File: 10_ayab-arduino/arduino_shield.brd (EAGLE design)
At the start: 69.9 x 54.6 mm, 20 parts, among them IC3 PCF8574T, IC4 PCF8574T

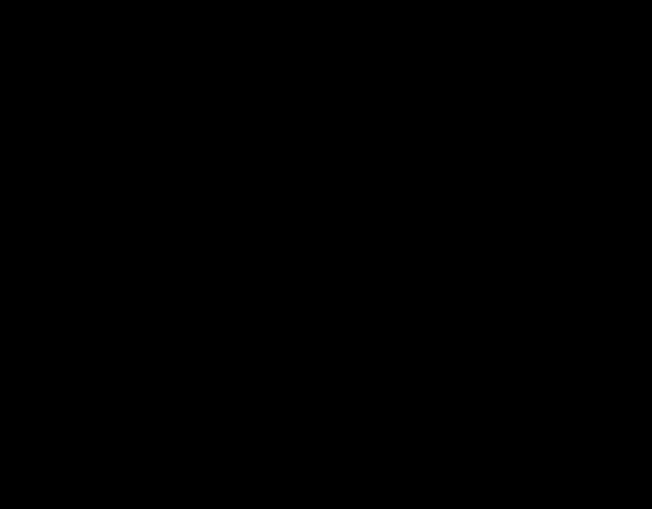
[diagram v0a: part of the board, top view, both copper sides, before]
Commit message: started work on improving shield, added reset button to schematic
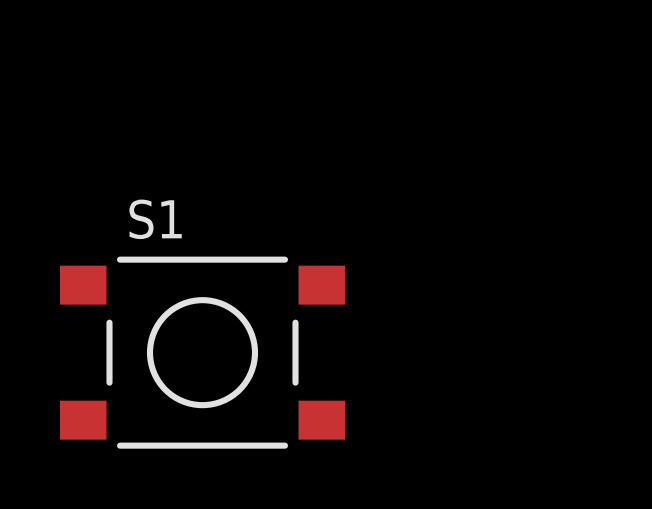
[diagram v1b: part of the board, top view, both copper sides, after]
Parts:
- added S1: DTSM-6, switch-tact:DTSM-6
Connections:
- new net RESET: ARD1.RST, S1.2
- net GND: now also S1.4
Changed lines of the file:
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@@
 <element name="U$1" library="frames" package="A4L-LOC" value="" x="-81.5975" y="-52.3875"/>
 <element name="JP6" library="pinhead" package="1X02" value="" x="39.0525" y="45.085" rot="R90"/>
+<element name="S1" library="switch-tact" package="DTSM-6" value="DTSM-6" x="-87.63" y="-47.625"/>
 </elements>
 <signals>
@@
 </signal>
 <signal name="GND">
-<contactref element="ARD1" pad="GND@1"/>
-<contactref element="ARD1" pad="GND@2"/>
-<contactref element="ARD1" pad="GND@3"/>
 <contactref element="IC3" pad="1"/>
 <contactref element="IC3" pad="2"/>
@@
 <contactref element="JP5" pad="10"/>
 <contactref element="LED1" pad="C"/>
-<contactref element="ARD1" pad="GND@1"/>
-<contactref element="ARD1" pad="GND@2"/>
 <contactref element="JP1" pad="P$2"/>
 <contactref element="JP1" pad="P$3"/>
@@
 <wire x1="18.0975" y1="8.255" x2="18.0975" y2="9.525" width="0.6096" layer="16"/>
 <wire x1="15.72" y1="7.62" x2="5.08" y2="7.62" width="0.6096" layer="16"/>
+<contactref element="ARD1" pad="GND@1"/>
+<contactref element="ARD1" pad="GND@2"/>
+<contactref element="ARD1" pad="GND@3"/>
+<contactref element="ARD1" pad="GND@1"/>
+<contactref element="ARD1" pad="GND@2"/>
+<contactref element="S1" pad="4"/>
+<wire x1="5.08" y1="7.62" x2="-83.655" y2="-49.875" width="0" layer="19" extent="1-1"/>
+<wire x1="5.08" y1="12.62" x2="5.08" y2="7.62" width="0" layer="19" extent="1-1"/>
+<wire x1="31.115" y1="22.86" x2="18.0975" y2="15.875" width="0" layer="19" extent="16-16"/>
+<wire x1="40.485" y1="16.51" x2="31.115" y2="22.86" width="0" layer="19" extent="16-16"/>
+<wire x1="40.64" y1="2.54" x2="40.485" y2="8.89" width="0" layer="19" extent="16-16"/>
+<wire x1="43.18" y1="2.54" x2="40.64" y2="2.54" width="0" layer="19" extent="1-1"/>
+<wire x1="55.88" y1="7.3025" x2="45.4025" y2="14.605" width="0" layer="19" extent="1-1"/>
+<wire x1="63.5" y1="10.34" x2="55.88" y2="7.3025" width="0" layer="19" extent="1-1"/>
+<wire x1="63.5" y1="12.84" x2="63.5" y2="10.34" width="0" layer="19" extent="1-1"/>
+<wire x1="63.5" y1="17.84" x2="63.5" y2="12.84" width="0" layer="19" extent="1-1"/>
+<wire x1="55.88" y1="22.86" x2="63.5" y2="17.84" width="0" layer="19" extent="1-1"/>
+<wire x1="63.5" y1="30.34" x2="55.88" y2="22.86" width="0" layer="19" extent="1-1"/>
+<wire x1="45.72" y1="46.77" x2="63.5" y2="30.34" width="0" layer="19" extent="1-1"/>
+<wire x1="26.416" y1="50.8" x2="45.72" y2="46.77" width="0" layer="19" extent="1-1"/>
 </signal>
 <signal name="+5V">
@@
 <wire x1="28.575" y1="20.955" x2="28.575" y2="22.86" width="0.6096" layer="16"/>
 </signal>
+<signal name="RESET">
+<contactref element="ARD1" pad="RST"/>
+<contactref element="S1" pad="2"/>
+<wire x1="33.02" y1="2.54" x2="-83.655" y2="-45.375" width="0" layer="19" extent="1-1"/>
+</signal>
 </signals>

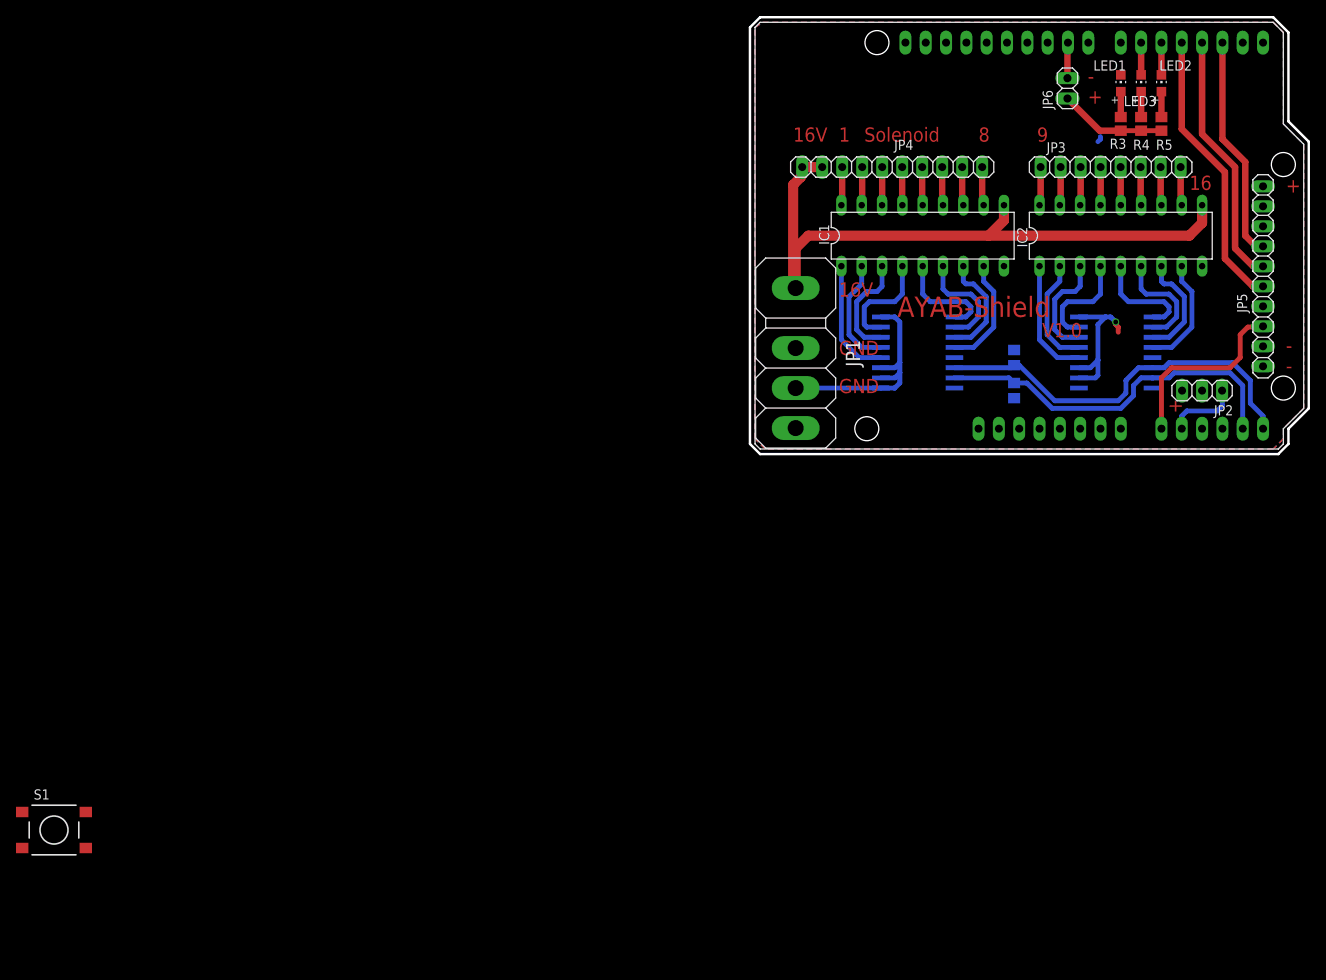
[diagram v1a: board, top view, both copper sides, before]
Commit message: added kh-930 specific connectors
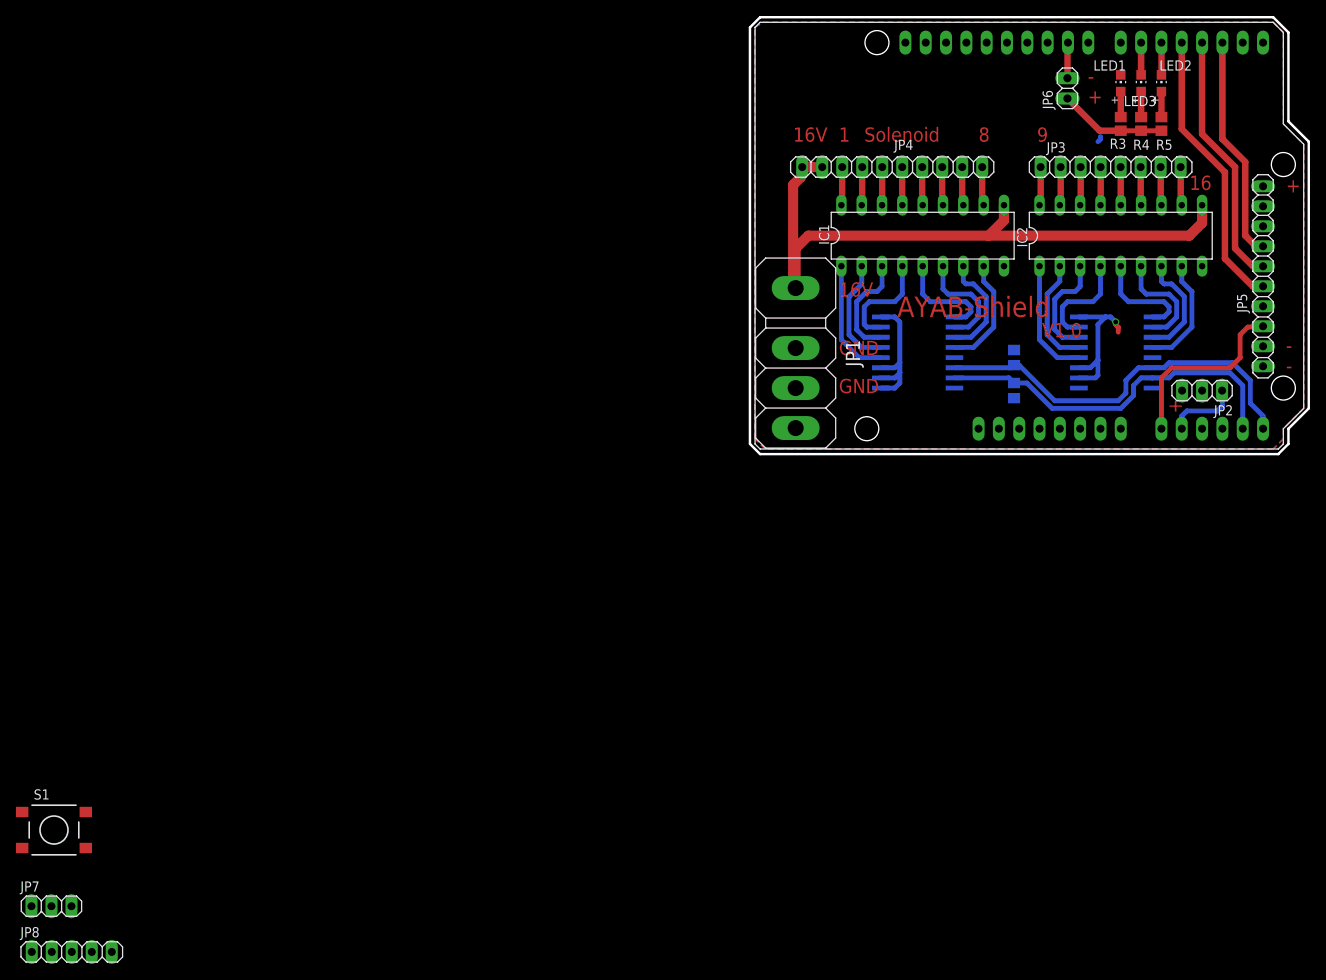
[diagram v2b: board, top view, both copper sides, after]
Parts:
- added JP7: (no value), pinheader_250:1X03
- added JP8: (no value), pinheader_250:1X05
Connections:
- net +5V: now also JP7.3, JP8.1
- net ENC0PINA: now also JP8.3
- net ENC0PINB: now also JP8.4
- net ENC0PINC: now also JP8.5
- net EOL0R: now also JP7.1
- net GND: now also JP7.2, JP8.2
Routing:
- net GND: track 48.1 -> 37.4 mm
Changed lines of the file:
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@@
 <element name="JP6" library="pinhead" package="1X02" value="" x="39.0525" y="45.085" rot="R90"/>
 <element name="S1" library="switch-tact" package="DTSM-6" value="DTSM-6" x="-87.63" y="-47.625"/>
+<element name="JP7" library="pinheader_250" package="1X03" value="" x="-87.9475" y="-57.15"/>
+<element name="JP8" library="pinheader_250" package="1X05" value="" x="-85.4075" y="-62.865"/>
 </elements>
 <signals>
@@
 <contactref element="IC3" pad="8"/>
 <contactref element="IC1" pad="9"/>
-<contactref element="JP2" pad="2"/>
 <contactref element="JP5" pad="2"/>
 <contactref element="JP5" pad="7"/>
@@
 <contactref element="JP5" pad="10"/>
 <contactref element="LED1" pad="C"/>
-<contactref element="JP1" pad="P$2"/>
-<contactref element="JP1" pad="P$3"/>
 <polygon width="0.6096" layer="1" isolate="0.4064">
 <vertex x="0" y="52.705"/>
@@
 <wire x1="17.4625" y1="7.62" x2="18.0975" y2="8.255" width="0.6096" layer="16"/>
 <wire x1="18.0975" y1="8.255" x2="18.0975" y2="9.525" width="0.6096" layer="16"/>
-<wire x1="15.72" y1="7.62" x2="5.08" y2="7.62" width="0.6096" layer="16"/>
 <contactref element="ARD1" pad="GND@1"/>
 <contactref element="ARD1" pad="GND@2"/>
@@
 <contactref element="ARD1" pad="GND@2"/>
 <contactref element="S1" pad="4"/>
+<contactref element="JP7" pad="2"/>
+<contactref element="JP2" pad="2"/>
+<contactref element="JP8" pad="2"/>
+<contactref element="JP1" pad="P$3"/>
+<contactref element="JP1" pad="P$2"/>
+<wire x1="-87.9475" y1="-57.15" x2="-87.9075" y2="-62.865" width="0" layer="19" extent="1-1"/>
+<wire x1="-83.655" y1="-49.875" x2="-87.9475" y2="-57.15" width="0" layer="19" extent="1-1"/>
 <wire x1="5.08" y1="7.62" x2="-83.655" y2="-49.875" width="0" layer="19" extent="1-1"/>
 <wire x1="5.08" y1="12.62" x2="5.08" y2="7.62" width="0" layer="19" extent="1-1"/>
+<wire x1="15.72" y1="7.62" x2="5.08" y2="7.62" width="0" layer="19" extent="16-16"/>
 <wire x1="31.115" y1="22.86" x2="18.0975" y2="15.875" width="0" layer="19" extent="16-16"/>
 <wire x1="40.485" y1="16.51" x2="31.115" y2="22.86" width="0" layer="19" extent="16-16"/>
@@
 <contactref element="R2" pad="2"/>
 <contactref element="IC4" pad="16"/>
-<contactref element="JP2" pad="3"/>
 <contactref element="JP5" pad="1"/>
 <contactref element="R3" pad="2"/>
@@
 <contactref element="ARD1" pad="IOREF"/>
 <contactref element="ARD1" pad="AREF"/>
+<contactref element="JP7" pad="3"/>
+<contactref element="JP2" pad="3"/>
+<contactref element="JP8" pad="1"/>
+<wire x1="-85.4475" y1="-57.15" x2="-90.4075" y2="-62.865" width="0" layer="19" extent="1-1"/>
+<wire x1="24.92" y1="7.62" x2="-85.4475" y2="-57.15" width="0" layer="19" extent="16-16"/>
+<wire x1="30.48" y1="2.54" x2="24.92" y2="7.62" width="0" layer="19" extent="16-16"/>
+<wire x1="32.385" y1="6.3525" x2="30.48" y2="2.54" width="0" layer="19" extent="16-16"/>
+<wire x1="32.385" y1="12.38" x2="32.385" y2="6.3525" width="0" layer="19" extent="16-16"/>
+<wire x1="38.1" y1="2.54" x2="32.385" y2="6.3525" width="0" layer="19" extent="16-16"/>
+<wire x1="40.485" y1="7.62" x2="38.1" y2="2.54" width="0" layer="19" extent="16-16"/>
+<wire x1="49.685" y1="7.62" x2="40.485" y2="7.62" width="0" layer="19" extent="16-16"/>
+<wire x1="53.38" y1="7.3025" x2="49.685" y2="7.62" width="0" layer="19" extent="16-16"/>
+<wire x1="63.5" y1="32.84" x2="53.38" y2="7.3025" width="0" layer="19" extent="1-1"/>
+<wire x1="50.8" y1="39.79" x2="63.5" y2="32.84" width="0" layer="19" extent="1-1"/>
+<wire x1="43.18" y1="39.0525" x2="43.0775" y2="39.79" width="0" layer="19" extent="1-16"/>
+<wire x1="23.876" y1="50.8" x2="39.0525" y2="43.815" width="0" layer="19" extent="1-1"/>
 </signal>
 <signal name="N$1">
@@
 <wire x1="61.2775" y1="26.67" x2="62.5475" y2="25.4" width="0.8128" layer="1"/>
 <wire x1="62.5475" y1="25.4" x2="63.5" y2="25.34" width="0.8128" layer="1"/>
+<contactref element="JP8" pad="3"/>
+<wire x1="61.2775" y1="26.67" x2="-85.4075" y2="-62.865" width="0" layer="19" extent="1-1"/>
 </signal>
 <signal name="ENC0PINB">
@@
 <wire x1="60.0075" y1="25.0825" x2="62.23" y2="22.86" width="0.8128" layer="1"/>
 <wire x1="62.23" y1="22.86" x2="63.5" y2="22.84" width="0.8128" layer="1"/>
+<contactref element="JP8" pad="4"/>
+<wire x1="60.0075" y1="25.0825" x2="-82.9075" y2="-62.865" width="0" layer="19" extent="1-1"/>
 </signal>
 <signal name="ENC0PINC">
@@
 <wire x1="58.7375" y1="23.8125" x2="62.23" y2="20.32" width="0.8128" layer="1"/>
 <wire x1="62.23" y1="20.32" x2="63.5" y2="20.34" width="0.8128" layer="1"/>
+<contactref element="JP8" pad="5"/>
+<wire x1="58.7375" y1="23.8125" x2="-80.4075" y2="-62.865" width="0" layer="19" extent="1-1"/>
 </signal>
 <signal name="EOL0R">
@@
 <wire x1="52.07" y1="10.16" x2="50.8" y2="8.89" width="0.6096" layer="1"/>
 <wire x1="50.8" y1="8.89" x2="50.8" y2="2.54" width="0.6096" layer="1"/>
+<contactref element="JP7" pad="1"/>
+<wire x1="50.8" y1="2.54" x2="-90.4475" y2="-57.15" width="0" layer="19" extent="1-1"/>
 </signal>
 <signal name="EOL0L">

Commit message: Finished Board Layout for v1.1
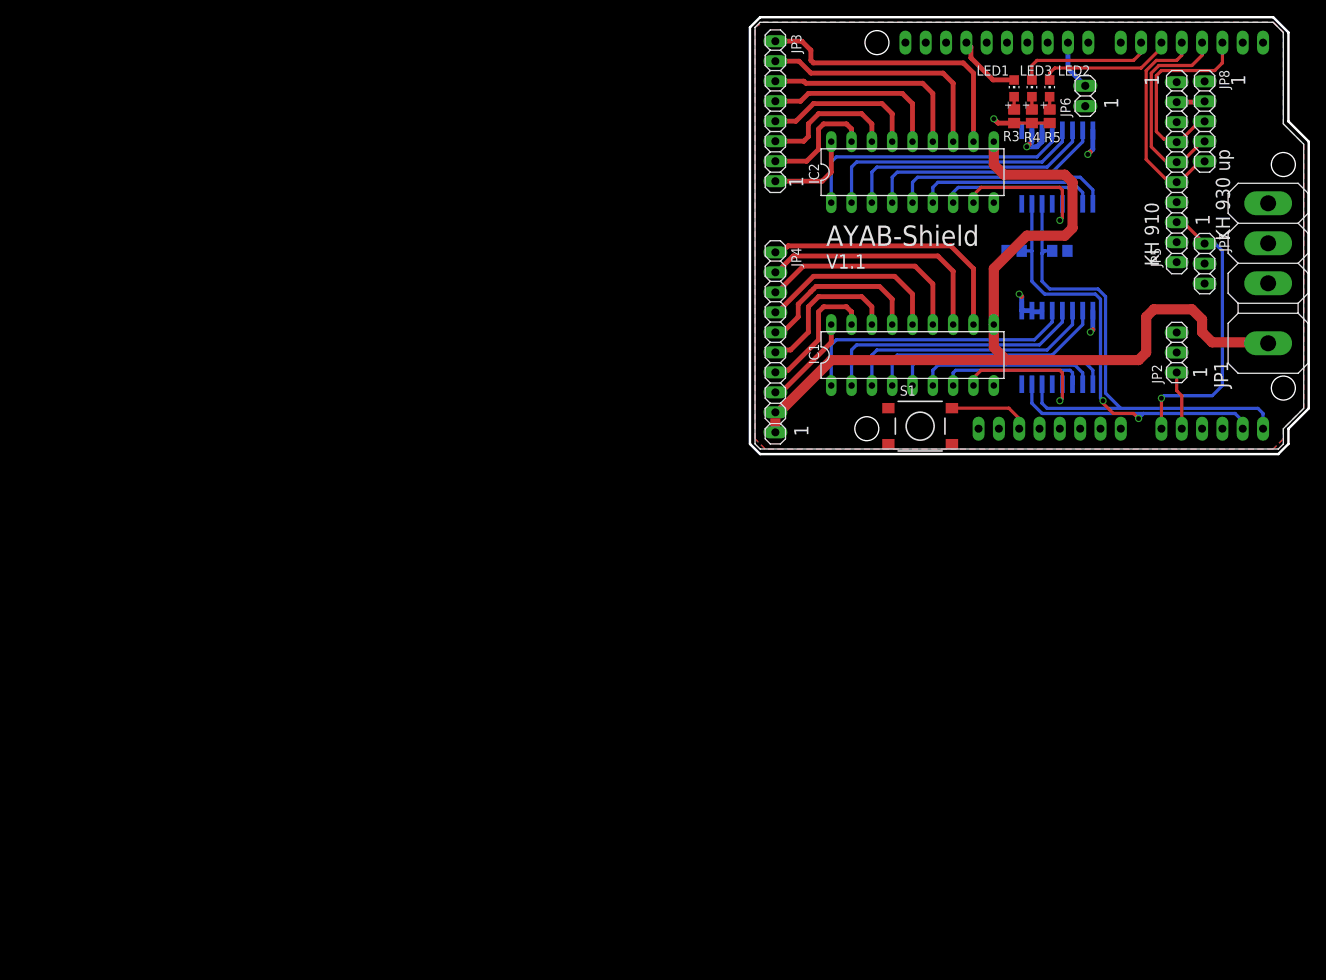
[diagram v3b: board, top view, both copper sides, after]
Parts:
- moved JP8 175.6 mm to (56.2, 41.0), turned to 270 degrees
- moved JP7 165.0 mm to (56.2, 23.2), turned to 270 degrees
- moved S1 119.5 mm to (20.6, 2.86)
- moved JP1 61.8 mm to (64.1, 25.7), turned to 270 degrees
- moved JP3 42.5 mm to (2.54, 42.2), turned to 90 degrees
- moved IC2 27.2 mm to (19.7, 34.6)
- moved JP4 26.3 mm to (2.54, 13.3), turned to 90 degrees
- moved IC4 24.3 mm to (37.8, 35.2), turned to 180 degrees
- moved IC3 17.5 mm to (37.8, 12.7), turned to 180 degrees
- moved R1 17.5 mm to (32.4, 24.8), turned to 0 degrees
- moved JP5 16.9 mm to (52.7, 34.6)
- moved IC1 15.0 mm to (19.7, 11.7)
- moved R2 14.5 mm to (38.1, 24.8), turned to 180 degrees
- moved R5 14.0 mm to (36.8, 41.6)
- moved LED2 14.0 mm to (36.8, 45.1)
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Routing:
- net +15V: track 82.1 -> 118.1 mm
- net N$24: track 4.82 -> 35.7 mm
- net N$25: track 4.84 -> 33.3 mm
- net N$26: track 4.82 -> 30.9 mm
- net N$23: track 4.80 -> 30.7 mm
- net SDA: track 46.3 -> 70.3 mm, vias 0 -> 2
- net N$27: track 4.80 -> 27.5 mm
- net N$22: track 4.79 -> 26.4 mm
- net N$2: track 15.1 -> 35.3 mm
- net N$1: track 15.1 -> 35.2 mm
- net N$3: track 13.9 -> 33.7 mm
- net N$10: track 13.9 -> 33.5 mm
- net N$28: track 4.79 -> 23.7 mm
- net N$4: track 13.4 -> 32.2 mm
- net N$11: track 13.6 -> 31.9 mm
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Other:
- board text added: "KH 910"
- board text added: "KH 930 up"
- board text added: "V1.1"
- board text removed: "+"
- board text removed: "-"
- board text removed: "16"
- board text removed: "16V"
- board text removed: "8"
- board text removed: "9"
- board text removed: "GND"
- board text removed: "Solenoid"
- board text removed: "V1.0"
